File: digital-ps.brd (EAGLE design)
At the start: 73.7 x 50.8 mm, 74 parts, among them CON1 SWD_CON, IC1 STM32F334K8, IC2 MCP14700, IC3 7805, IC4 7805, IC5 S812, Q1 40V, Q2 40V

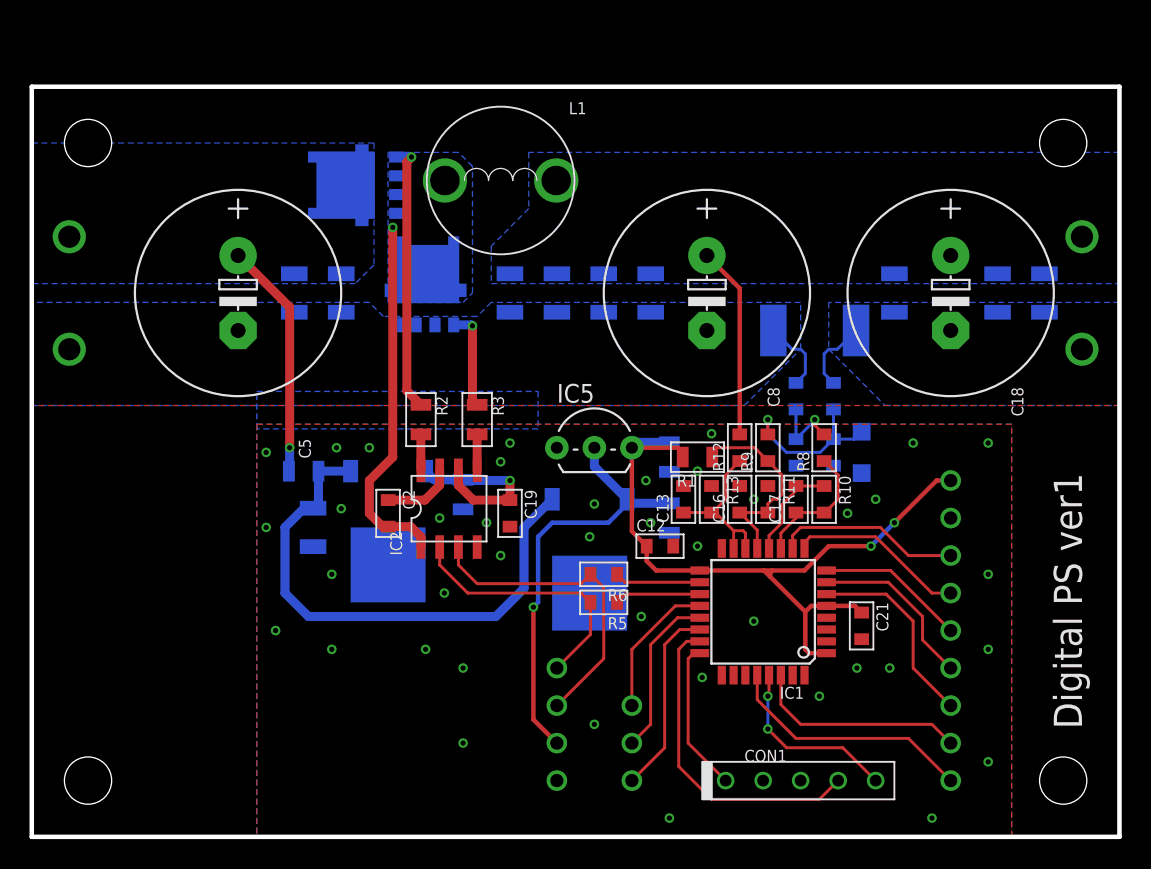
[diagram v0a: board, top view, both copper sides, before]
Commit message: FETのゲート逆だった
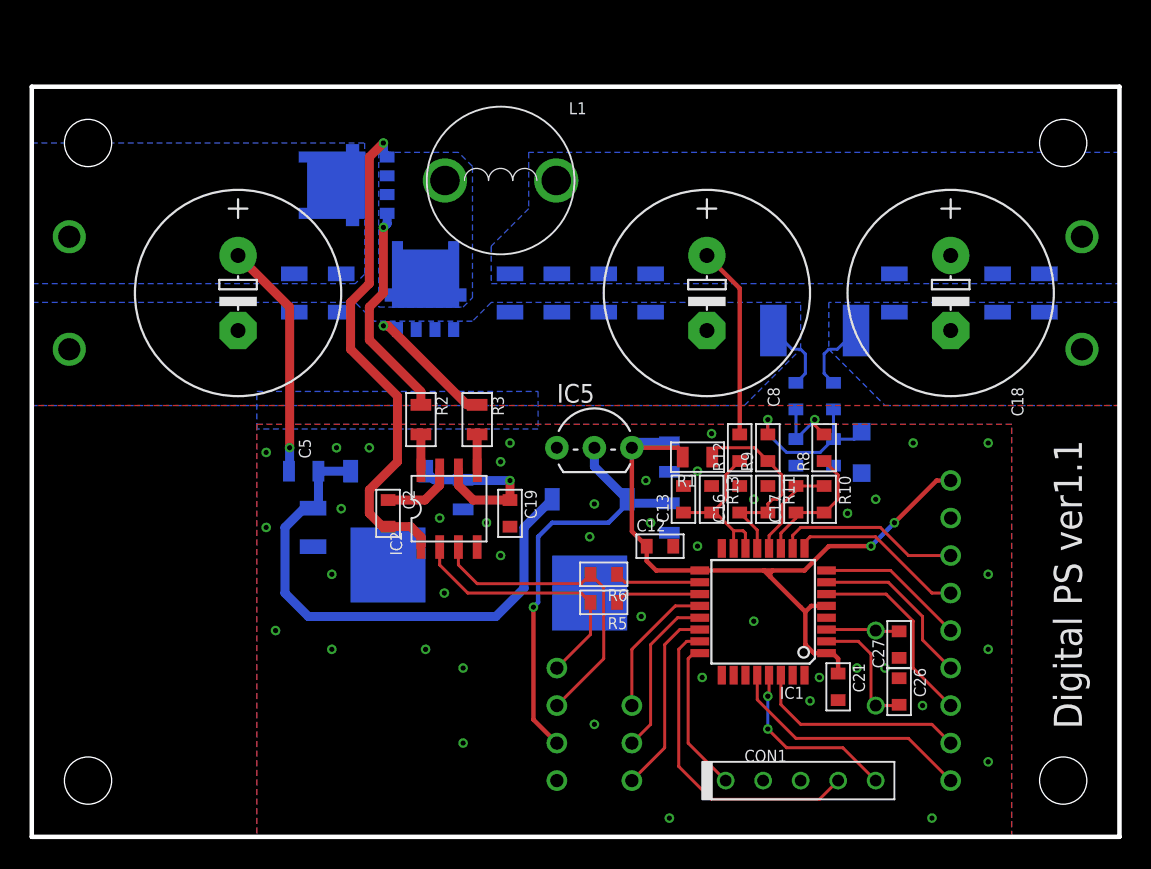
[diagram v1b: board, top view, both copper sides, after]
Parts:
- added C26, C27: 10p, my_rcl:1608
- added X1: 12MHz, my_rcl:HC49/S
- moved C21 4.42 mm to (54.6, 10.2)
- moved Q1 0.63 mm to (21.3, 44.1)
- moved Q2 0.32 mm to (26.7, 37.1)
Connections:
- new net N$24: C26.2, IC1.2, X1.1
- new net N$25: C27.2, IC1.3, X1.2
- net GND: now also C26.1, C27.1, Q2.1; no longer Q2.4
- net N$10: now also Q2.4; no longer Q2.1
- net N$9: now also Q1.4; no longer Q1.1
- net SW: now also Q1.1; no longer Q1.4
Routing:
- net SW: track 24.9 -> 34.1 mm
- net N$24: track 0.00 -> 8.60 mm
- net N$25: track 0.00 -> 4.97 mm
- net N$9: track 18.3 -> 14.9 mm
- net N$10: track 6.78 -> 9.62 mm
- net +3V3: track 50.7 -> 49.9 mm
- net GND: vias 41 -> 43
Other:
- board text added: "Digital PS ver1.1"
- board text removed: "Digital PS ver1"

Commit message: F303 GaN FET
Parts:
- removed TP14: PA10, my_connector:TESTPIN
- added C28: 0.1u, my_rcl:1608
- added R16, R4: 10k, my_rcl:2012
- added TP21: PA15, my_connector:TESTPIN
- added TP22: PB3, my_connector:TESTPIN
- added TP23: PB4, my_connector:TESTPIN
- C6: value 10u -> 1u; device my_rcl:3216 -> my_rcl:2012
- FB1: device my_rcl:2012 -> my_rcl:2012-J
- IC1: value STM32F334K8 -> STM32F303K8T6
- IC5: value S812 -> 3.3V; device my_ic:TO-92 -> my_ic:P-HSIP3_2.30A
- Q1: value 40V -> EPC2052; device my_ic:DFN5_5X6 -> my_ic:EPC2052
- Q2: value 40V -> (none); device my_ic:DFN5_5X6 -> my_ic:EPC2052
- R7: value 100m -> 40m
- moved IC4 17.8 mm to (24.1, 11.4)
- moved C9 13.3 mm to (19.1, 36.8)
- moved Q1 8.33 mm to (26.7, 37.8), turned to 270 degrees
- moved C3 8.01 mm to (36.5, 26.0), turned to 180 degrees
- moved C7 4.13 mm to (21.9, 36.8)
- moved C6 3.49 mm to (24.4, 36.8)
- moved IC5 3.01 mm to (39.1, 23.5), flipped to the bottom, turned to 180 degrees
- moved C4 2.56 mm to (40.6, 26.0), turned to 0 degrees
- moved Q2 1.59 mm to (26.7, 35.6), turned to 90 degrees
- moved L1 1.27 mm to (33.0, 44.5)
- moved TP13 1.27 mm to (40.6, 7.62)
- moved TP12 1.27 mm to (40.6, 5.08)
- moved TP17 1.27 mm to (35.6, 2.54)
- moved TP16 1.27 mm to (35.6, 5.08)
- moved TP19 1.27 mm to (35.6, 10.2)
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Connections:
- removed net N$2: IC1.19, R5.1
- new net N$23: IC1.27, TP23.1
- new net N$26: IC1.26, TP22.1
- new net N$27: IC1.25, TP21.1
- net +3V3: now also C28.1
- net +5V: now also IC5.1; no longer IC5.2
- net GND: now also C28.2, IC5.2, Q2.7, Q2.8, Q2.9, R16.1; no longer IC5.1, Q2.1
- net N$10: now also Q2.1, R16.2; no longer Q2.4
- net N$20: now also R5.1; no longer TP14.1
- net N$9: now also Q1.1, R4.2; no longer Q1.4
- net OUT+: no longer C9.1
- net SW: now also Q1.7, Q1.8, Q1.9, Q2.4, Q2.5, Q2.6, R4.1; no longer Q1.1, Q2.5_6, Q2.5_6_1, Q2.5_6_2, Q2.5_6_3, Q2.5_6_4
- net VP: now also C9.1, Q1.4, Q1.5, Q1.6; no longer Q1.5_6, Q1.5_6_1, Q1.5_6_2, Q1.5_6_3, Q1.5_6_4
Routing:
- net VCC: track 36.2 -> 19.0 mm
- net N$23: track 0.00 -> 15.3 mm, vias 0 -> 1
- net N$26: track 0.00 -> 13.5 mm, vias 0 -> 1
- net N$27: track 0.00 -> 7.29 mm, vias 0 -> 1
- net N$2: track 5.84 -> 0.00 mm
- net GND: track 5.31 -> 9.57 mm, vias 43 -> 72
- net N$20: track 9.63 -> 5.70 mm
- net +5V: track 29.3 -> 32.8 mm, vias 1 -> 0
- net VP: track 16.1 -> 18.8 mm
- net SW: track 34.1 -> 36.4 mm
- net PWML: track 21.5 -> 20.2 mm
- net N$22: track 12.9 -> 11.7 mm
- net N$21: track 11.3 -> 10.0 mm
- net PWMH: track 17.9 -> 16.6 mm
- net +3V3: track 49.9 -> 48.7 mm, vias 2 -> 3
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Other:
- board text added: "Digital PS ver0.2"
- board text removed: "Digital PS ver1.1"

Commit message: 微修正
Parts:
- moved C3 0.95 mm to (37.5, 26.0)
- moved C4 0.95 mm to (41.6, 26.0)
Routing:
- net GND: vias 72 -> 75
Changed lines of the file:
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@@
 <attribute name="VALUE" x="22.33" y="23.19" size="0.8128" layer="27" rot="R270"/>
 </element>
-<element name="C3" library="my_rcl" package="2012" value="10u" x="36.5125" y="26.035" smashed="yes" rot="MR180">
-<attribute name="NAME" x="35.1125" y="28.035" size="0.8128" layer="26" rot="MR180"/>
-<attribute name="VALUE" x="35.43" y="28.1275" size="0.8128" layer="28" rot="MR180"/>
-</element>
-<element name="C4" library="my_rcl" package="2012" value="10u" x="40.64" y="26.035" smashed="yes" rot="MR0">
-<attribute name="NAME" x="42.04" y="24.035" size="0.8128" layer="26" rot="MR0"/>
-<attribute name="VALUE" x="41.7225" y="23.9425" size="0.8128" layer="28" rot="MR0"/>
+<element name="C3" library="my_rcl" package="2012" value="10u" x="37.465" y="26.035" smashed="yes" rot="MR180">
+<attribute name="NAME" x="36.065" y="28.035" size="0.8128" layer="26" rot="MR180"/>
+<attribute name="VALUE" x="36.3825" y="28.1275" size="0.8128" layer="28" rot="MR180"/>
+</element>
+<element name="C4" library="my_rcl" package="2012" value="10u" x="41.5925" y="26.035" smashed="yes" rot="MR0">
+<attribute name="NAME" x="42.9925" y="24.035" size="0.8128" layer="26" rot="MR0"/>
+<attribute name="VALUE" x="40.51" y="28.1275" size="0.8128" layer="28" rot="MR180"/>
 </element>
 <element name="C5" library="my_rcl" package="E5-13" value="1000u" x="13.97" y="36.83" smashed="yes" rot="R270">
@@
 <via x="50.8" y="12.7" extent="1-16" drill="0.35"/>
 <contactref element="R16" pad="1"/>
+<via x="40.64" y="27.6225" extent="1-16" drill="0.35"/>
+<via x="34.29" y="21.59" extent="1-16" drill="0.35"/>
+<via x="34.29" y="24.13" extent="1-16" drill="0.35"/>
 </signal>
 <signal name="+3V3">
@@
 <contactref element="C28" pad="1"/>
 <contactref element="IC5" pad="3"/>
-<wire x1="41.64" y1="26.035" x2="41.5925" y2="25.9875" width="0.6096" layer="16"/>
-<wire x1="41.5925" y1="25.9875" x2="41.5925" y2="23.495" width="0.6096" layer="16"/>
+<wire x1="42.5925" y1="26.035" x2="41.5925" y2="25.035" width="0.6096" layer="16"/>
+<wire x1="41.5925" y1="25.035" x2="41.5925" y2="23.495" width="0.6096" layer="16"/>
 <wire x1="41.5925" y1="23.495" x2="41.5925" y2="21.9075" width="0.6096" layer="16"/>
 <via x="41.5925" y="21.9075" extent="1-16" drill="0.35"/>
@@
 <wire x1="34.29" y1="15.24" x2="34.29" y2="19.685" width="0.6096" layer="16"/>
 <wire x1="36.5125" y1="23.495" x2="36.5125" y2="23.765" width="0.6096" layer="16"/>
-<wire x1="36.5125" y1="23.765" x2="35.5125" y2="24.765" width="0.6096" layer="16"/>
-<wire x1="35.5125" y1="24.765" x2="35.5125" y2="26.035" width="0.6096" layer="16"/>
+<wire x1="36.5125" y1="23.765" x2="36.465" y2="23.8125" width="0.6096" layer="16"/>
+<wire x1="36.465" y1="23.8125" x2="36.465" y2="26.035" width="0.6096" layer="16"/>
 <wire x1="35.56" y1="5.08" x2="33.02" y2="5.08" width="0.8128" layer="16"/>
 <wire x1="33.02" y1="5.08" x2="26.67" y2="11.43" width="0.8128" layer="16"/>

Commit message: 発注
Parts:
- added C29: 1n, my_rcl:1608
- added R17: 10, my_rcl:2012
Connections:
- new net N$2: C29.1, R17.1
- net GND: now also C29.2
- net SW: now also R17.2
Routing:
- net N$2: track 0.00 -> 1.91 mm
- net SW: track 36.4 -> 37.3 mm
- net GND: track 9.57 -> 8.78 mm
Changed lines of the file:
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@@
 <attribute name="VALUE" x="33.4675" y="31.3025" size="0.8128" layer="27" rot="R180"/>
+</element>
+<element name="R17" library="my_rcl" package="2012" value="10" x="30.1625" y="36.195" smashed="yes" rot="MR90">
+<attribute name="NAME" x="28.1625" y="34.795" size="0.8128" layer="26" rot="MR90"/>
+</element>
+<element name="C29" library="my_rcl" package="1608" value="1n" x="32.0675" y="34.29" smashed="yes" rot="MR270">
+<attribute name="NAME" x="31.0675" y="35.89" size="0.8128" layer="26" rot="MR270"/>
 </element>
 </elements>
@@
 <contactref element="Q2" pad="8"/>
 <contactref element="Q2" pad="9"/>
-<wire x1="26.22" y1="35.11" x2="25.85" y2="35.11" width="0.2032" layer="16"/>
-<wire x1="25.85" y1="35.11" x2="25.7175" y2="35.2425" width="0.2032" layer="16"/>
-<wire x1="25.7175" y1="35.2425" x2="25.7175" y2="36.01" width="0.2032" layer="16"/>
-<wire x1="25.7175" y1="36.01" x2="24.6275" y2="36.01" width="0.2032" layer="16"/>
-<wire x1="24.6275" y1="36.01" x2="24.4475" y2="35.83" width="0.2032" layer="16"/>
 <polygon width="0.3048" layer="16" thermals="no">
 <vertex x="25.7175" y="29.21"/>
@@
 <vertex x="48.26" y="29.21"/>
 </polygon>
-<wire x1="26.67" y1="35.11" x2="26.22" y2="35.11" width="0.2032" layer="16"/>
-<wire x1="27.12" y1="36.01" x2="26.67" y2="36.01" width="0.2032" layer="16"/>
-<wire x1="26.22" y1="36.01" x2="25.7175" y2="36.01" width="0.2032" layer="16"/>
-<wire x1="26.22" y1="36.01" x2="26.67" y2="36.01" width="0.2032" layer="16"/>
 <contactref element="C9" pad="2"/>
 <contactref element="C28" pad="2"/>
@@
 <via x="34.29" y="21.59" extent="1-16" drill="0.35"/>
 <via x="34.29" y="24.13" extent="1-16" drill="0.35"/>
+<contactref element="C29" pad="2"/>
+<wire x1="26.67" y1="35.11" x2="26.22" y2="35.11" width="0.2286" layer="16"/>
+<wire x1="26.22" y1="35.11" x2="25.5325" y2="35.11" width="0.2286" layer="16"/>
+<wire x1="25.5325" y1="35.11" x2="25.4" y2="35.2425" width="0.2286" layer="16"/>
+<wire x1="25.4" y1="35.2425" x2="25.4" y2="35.8775" width="0.2286" layer="16"/>
+<wire x1="25.4" y1="35.8775" x2="25.5325" y2="36.01" width="0.2286" layer="16"/>
+<wire x1="25.5325" y1="36.01" x2="26.22" y2="36.01" width="0.2286" layer="16"/>
+<wire x1="26.22" y1="36.01" x2="26.67" y2="36.01" width="0.2286" layer="16"/>
+<wire x1="26.67" y1="36.01" x2="27.12" y2="36.01" width="0.2286" layer="16"/>
 </signal>
 <signal name="+3V3">
@@
 <contactref element="R2" pad="1"/>
 <contactref element="Q1" pad="1"/>
-<wire x1="26.22" y1="38.920009375" x2="26.22" y2="38.2325" width="0.2032" layer="16"/>
 <via x="26.67" y="39.37" extent="1-16" drill="0.35"/>
 <wire x1="25.7175" y1="29.2575" x2="25.7175" y2="38.4175" width="0.6096" layer="1"/>
 <wire x1="25.7175" y1="38.4175" x2="26.67" y2="39.37" width="0.6096" layer="1"/>
-<wire x1="26.67" y1="39.37" x2="26.220009375" y2="38.920009375" width="0.2032" layer="16"/>
-<wire x1="26.220009375" y1="38.920009375" x2="26.22" y2="38.920009375" width="0.2032" layer="16"/>
 <contactref element="R4" pad="2"/>
 <wire x1="27.94" y1="29.2575" x2="25.7175" y2="29.2575" width="0.6096" layer="1"/>
+<wire x1="26.22" y1="38.2325" x2="26.22" y2="38.92" width="0.2286" layer="16"/>
+<wire x1="26.22" y1="38.92" x2="26.67" y2="39.37" width="0.2286" layer="16"/>
 </signal>
 <signal name="N$10">
@@
 <contactref element="Q2" pad="1"/>
 <wire x1="30.115" y1="29.2575" x2="30.1625" y2="29.2575" width="0.6096" layer="1"/>
-<wire x1="28.2575" y1="34.925" x2="28.0725" y2="35.11" width="0.2032" layer="16"/>
-<wire x1="27.12" y1="35.11" x2="28.0725" y2="35.11" width="0.2032" layer="16"/>
-<via x="28.2575" y="34.925" extent="1-16" drill="0.35"/>
+<via x="28.2575" y="34.6075" extent="1-16" drill="0.35"/>
 <wire x1="28.2575" y1="31.115" x2="30.115" y2="29.2575" width="0.6096" layer="1"/>
-<wire x1="28.2575" y1="34.925" x2="28.2575" y2="31.115" width="0.6096" layer="1"/>
+<wire x1="28.2575" y1="34.6075" x2="28.2575" y2="31.115" width="0.6096" layer="1"/>
 <contactref element="R16" pad="2"/>
 <wire x1="30.1625" y1="29.2575" x2="32.385" y2="29.2575" width="0.6096" layer="1"/>
+<wire x1="27.12" y1="35.11" x2="27.6225" y2="34.6075" width="0.2286" layer="16"/>
+<wire x1="27.6225" y1="34.6075" x2="28.2575" y2="34.6075" width="0.2286" layer="16"/>
 </signal>
 <signal name="SW">
@@
 <contactref element="Q1" pad="8"/>
 <contactref element="Q1" pad="9"/>
-<wire x1="27.6225" y1="38.1" x2="27.6225" y2="37.465" width="0.2032" layer="16"/>
-<wire x1="27.6225" y1="37.465" x2="27.6225" y2="35.56" width="0.2032" layer="16"/>
-<wire x1="27.6225" y1="35.56" x2="27.12" y2="35.56" width="0.2032" layer="16"/>
 <polygon width="0.3048" layer="16" thermals="no">
 <vertex x="31.75" y="46.355"/>
@@
 <wire x1="24.4475" y1="25.0825" x2="24.4475" y2="28.2575" width="0.6096" layer="1"/>
 <wire x1="24.4475" y1="28.2575" x2="24.4475" y2="39.0525" width="0.6096" layer="1"/>
-<wire x1="26.22" y1="35.56" x2="26.67" y2="35.56" width="0.2032" layer="16"/>
-<wire x1="26.67" y1="35.56" x2="27.12" y2="35.56" width="0.2032" layer="16"/>
-<wire x1="27.12" y1="37.3325" x2="26.67" y2="37.3325" width="0.2032" layer="16"/>
-<wire x1="26.67" y1="37.3325" x2="26.22" y2="37.3325" width="0.2032" layer="16"/>
-<wire x1="27.12" y1="38.2325" x2="26.67" y2="38.2325" width="0.2032" layer="16"/>
-<wire x1="27.12" y1="38.2325" x2="27.49" y2="38.2325" width="0.2032" layer="16"/>
-<wire x1="27.49" y1="38.2325" x2="27.6225" y2="38.1" width="0.2032" layer="16"/>
-<wire x1="27.12" y1="37.3325" x2="27.49" y2="37.3325" width="0.2032" layer="16"/>
-<wire x1="27.49" y1="37.3325" x2="27.6225" y2="37.465" width="0.2032" layer="16"/>
 <contactref element="R4" pad="1"/>
 <wire x1="27.94" y1="27.2575" x2="26.94" y2="28.2575" width="0.6096" layer="1"/>
 <wire x1="26.94" y1="28.2575" x2="24.4475" y2="28.2575" width="0.6096" layer="1"/>
+<contactref element="R17" pad="2"/>
+<wire x1="27.94" y1="35.56" x2="27.94" y2="37.465" width="0.2286" layer="16"/>
+<wire x1="27.94" y1="37.465" x2="27.94" y2="38.1" width="0.2286" layer="16"/>
+<wire x1="27.94" y1="38.1" x2="27.8075" y2="38.2325" width="0.2286" layer="16"/>
+<wire x1="27.8075" y1="38.2325" x2="27.12" y2="38.2325" width="0.2286" layer="16"/>
+<wire x1="27.12" y1="37.3325" x2="27.8075" y2="37.3325" width="0.2286" layer="16"/>
+<wire x1="27.8075" y1="37.3325" x2="27.94" y2="37.465" width="0.2286" layer="16"/>
+<wire x1="27.12" y1="37.3325" x2="26.67" y2="37.3325" width="0.2286" layer="16"/>
+<wire x1="26.67" y1="37.3325" x2="26.22" y2="37.3325" width="0.2286" layer="16"/>
+<wire x1="26.67" y1="38.2325" x2="27.12" y2="38.2325" width="0.2286" layer="16"/>
+<wire x1="26.22" y1="35.56" x2="26.67" y2="35.56" width="0.254" layer="16"/>
+<wire x1="26.67" y1="35.56" x2="27.12" y2="35.56" width="0.254" layer="16"/>
+<wire x1="27.12" y1="35.56" x2="27.94" y2="35.56" width="0.254" layer="16"/>
 </signal>
 <signal name="N$6">
@@
 <wire x1="17.4625" y1="35.8775" x2="17.4625" y2="26.3525" width="0.6096" layer="1"/>
 <via x="17.4625" y="26.3525" extent="1-16" drill="0.35"/>
-<wire x1="24.495" y1="37.7825" x2="24.4475" y2="37.83" width="0.2032" layer="16"/>
 <polygon width="0.3048" layer="16" thermals="no">
 <vertex x="25.7175" y="37.1475"/>
@@
 <vertex x="25.7175" y="43.18"/>
 </polygon>
-<wire x1="27.12" y1="37.7825" x2="26.67" y2="37.7825" width="0.2032" layer="16"/>
-<wire x1="26.67" y1="37.7825" x2="26.22" y2="37.7825" width="0.2032" layer="16"/>
-<wire x1="26.22" y1="37.7825" x2="24.495" y2="37.7825" width="0.2032" layer="16"/>
 <contactref element="C9" pad="1"/>
 <wire x1="17.615" y1="24.765" x2="17.4625" y2="24.9175" width="0.6096" layer="16"/>
 <wire x1="17.4625" y1="24.9175" x2="17.4625" y2="26.3525" width="0.6096" layer="16"/>
+<wire x1="27.12" y1="37.7825" x2="26.67" y2="37.7825" width="0.254" layer="16"/>
+<wire x1="26.67" y1="37.7825" x2="26.22" y2="37.7825" width="0.254" layer="16"/>
+<wire x1="26.22" y1="37.7825" x2="24.495" y2="37.7825" width="0.254" layer="16"/>
+<wire x1="24.495" y1="37.7825" x2="24.4475" y2="37.83" width="0.254" layer="16"/>
 </signal>
 <signal name="+5V">
@@
 <wire x1="46.73" y1="10.9474" x2="46.73" y2="9.9" width="0.2032" layer="1"/>
 </signal>
+<signal name="N$2">
+<contactref element="R17" pad="1"/>
+<contactref element="C29" pad="1"/>
+<wire x1="30.1625" y1="35.195" x2="32.0625" y2="35.195" width="0.6096" layer="16"/>
+<wire x1="32.0625" y1="35.195" x2="32.0675" y2="35.19" width="0.6096" layer="16"/>
+</signal>
 </signals>
